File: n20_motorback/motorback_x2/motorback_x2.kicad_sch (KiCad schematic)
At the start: 13 parts, among them J1 Servo wire input, J2 Conn_01x01_Male, J3 Conn_01x01_Male, J4 prog_pins, U1 DRV8837DSGR, U2 ATtiny4-TS, U3 AIC1734-33GUTR

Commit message: mechanical improvements
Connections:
- net MOTORF: now also J4.5 (Pin_5), U2.1 (PB0); no longer J4.4 (Pin_4), U2.3 (PB1)
- net MOTORR: now also J4.4 (Pin_4), U2.3 (PB1); no longer J4.5 (Pin_5), U2.1 (PB0)
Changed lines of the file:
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@@
-    (stroke (width 0) (type solid) (color 0 0 0 0))
-  )
-  (wire (pts (xy 171.45 82.55) (xy 185.42 82.55))
     (stroke (width 0) (type solid) (color 0 0 0 0))
   )
@@
     (stroke (width 0) (type solid) (color 0 0 0 0))
   )
-  (wire (pts (xy 184.15 81.28) (xy 184.15 85.09))
+  (wire (pts (xy 180.975 81.28) (xy 180.975 82.55))
     (stroke (width 0) (type solid) (color 0 0 0 0))
   )
-  (wire (pts (xy 184.15 81.28) (xy 207.01 81.28))
+  (wire (pts (xy 180.975 81.28) (xy 207.01 81.28))
+    (stroke (width 0) (type solid) (color 0 0 0 0))
+  )
+  (wire (pts (xy 180.975 82.55) (xy 171.45 82.55))
+    (stroke (width 0) (type solid) (color 0 0 0 0))
+  )
+  (wire (pts (xy 184.15 83.82) (xy 184.15 85.09))
+    (stroke (width 0) (type solid) (color 0 0 0 0))
+  )
+  (wire (pts (xy 184.15 83.82) (xy 207.01 83.82))
     (stroke (width 0) (type solid) (color 0 0 0 0))
   )
   (wire (pts (xy 184.15 85.09) (xy 171.45 85.09))
-    (stroke (width 0) (type solid) (color 0 0 0 0))
-  )
-  (wire (pts (xy 185.42 82.55) (xy 185.42 83.82))
-    (stroke (width 0) (type solid) (color 0 0 0 0))
-  )
-  (wire (pts (xy 185.42 83.82) (xy 207.01 83.82))
     (stroke (width 0) (type solid) (color 0 0 0 0))
   )
@@
     (stroke (width 0) (type solid) (color 0 0 0 0))
   )
-  (text "PB0/ " (at 52.705 81.28 180)
+  (text "PB1/ " (at 53.34 81.28 180)
     (effects (font (size 1.27 1.27)) (justify right bottom))
   )
-  (text "PB1/ " (at 53.975 83.82 180)
+  (text "PB0/ " (at 53.34 83.82 180)
     (effects (font (size 1.27 1.27)) (justify right bottom))
   )
@@
     (effects (font (size 1.27 1.27)) (justify right bottom))
   )
-  (label "MOTORR" (at 45.72 81.28 180)
+  (label "MOTORF" (at 45.72 81.28 180)
     (effects (font (size 1.27 1.27)) (justify right bottom))
   )
-  (label "MOTORF" (at 46.355 83.82 180)
+  (label "MOTORR" (at 46.355 83.82 180)
     (effects (font (size 1.27 1.27)) (justify right bottom))
   )

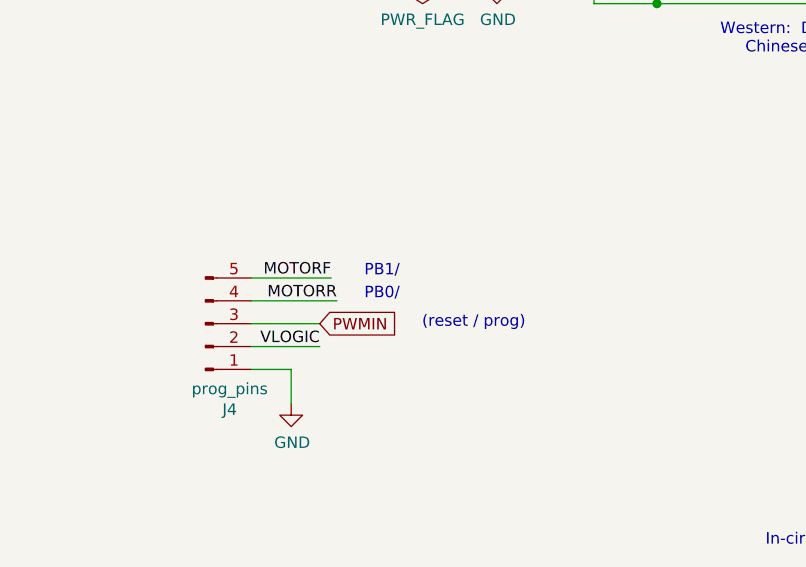
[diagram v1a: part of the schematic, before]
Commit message: Correct tpiclk / tpidata confusion
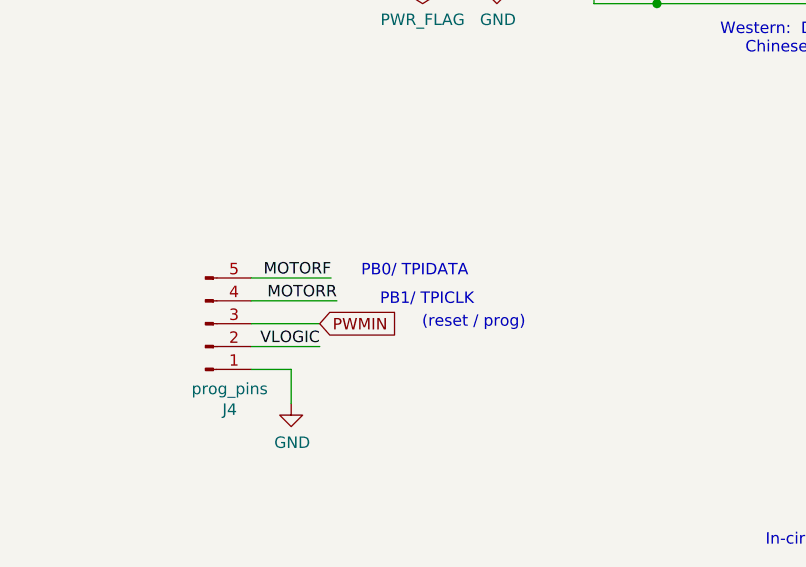
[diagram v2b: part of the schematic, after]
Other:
- note added: "PB0/ TPIDATA"
- note added: "PB1/ TPICLK"
- note removed: "PB0/"
- note removed: "PB1/"
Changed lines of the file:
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@@
     (stroke (width 0) (type solid) (color 0 0 0 0))
-  )
-  (text "PB1/ " (at 53.34 81.28 180)
-    (effects (font (size 1.27 1.27)) (justify right bottom))
-  )
-  (text "PB0/ " (at 53.34 83.82 180)
-    (effects (font (size 1.27 1.27)) (justify right bottom))
   )
   (text "Input servo connector" (at 55.88 33.02 180)
     (effects (font (size 1.27 1.27)) (justify right bottom))
   )
+  (text "PB0/ TPIDATA" (at 60.96 81.28 180)
+    (effects (font (size 1.27 1.27)) (justify right bottom))
+  )
+  (text "PB1/ TPICLK " (at 61.595 84.455 180)
+    (effects (font (size 1.27 1.27)) (justify right bottom))
+  )

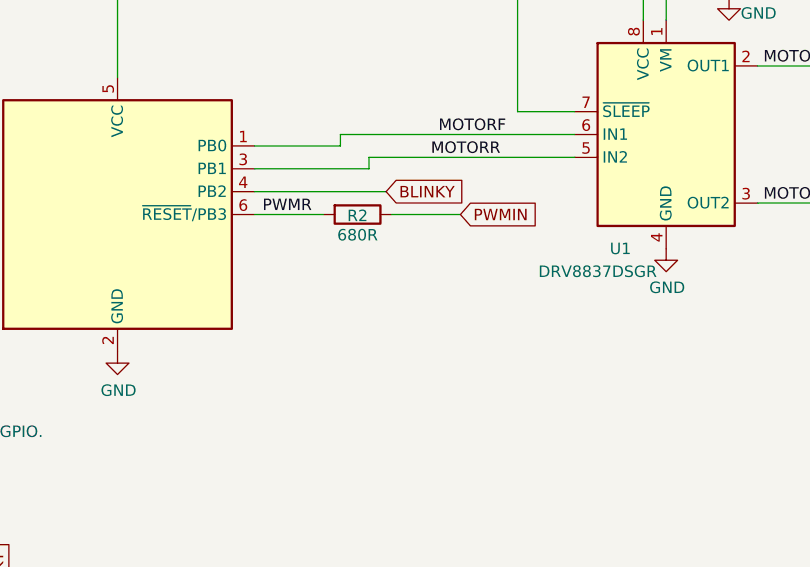
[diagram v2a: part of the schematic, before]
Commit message: Optional pull-down resistor
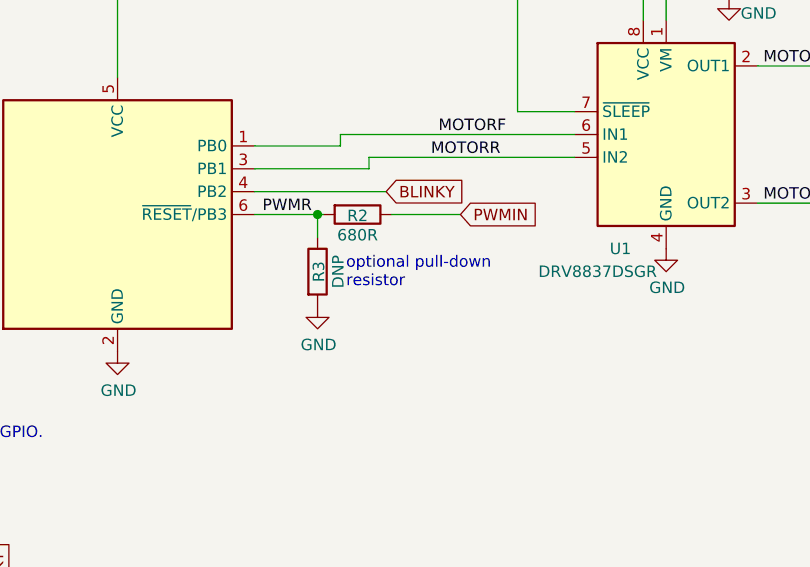
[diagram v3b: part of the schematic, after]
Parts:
- added R3: DNP, Resistor_SMD:R_0603_1608Metric, symbol Device:R
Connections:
- net GND: now also R3.2
- net PWMR: now also R3.1
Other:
- note added: "optional pull-down resistor"
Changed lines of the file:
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@@
   (junction (at 101.6 50.8) (diameter 1.016) (color 0 0 0 0))
   (junction (at 114.3 43.18) (diameter 1.016) (color 0 0 0 0))
+  (junction (at 178.435 90.17) (diameter 1.016) (color 0 0 0 0))
   (junction (at 200.66 63.5) (diameter 1.016) (color 0 0 0 0))
   (junction (at 224.155 58.42) (diameter 1.016) (color 0 0 0 0))
@@
     (stroke (width 0) (type solid) (color 0 0 0 0))
   )
-  (wire (pts (xy 171.45 90.17) (xy 179.07 90.17))
+  (wire (pts (xy 171.45 90.17) (xy 178.435 90.17))
+    (stroke (width 0) (type solid) (color 0 0 0 0))
+  )
+  (wire (pts (xy 178.435 90.17) (xy 178.435 92.71))
+    (stroke (width 0) (type solid) (color 0 0 0 0))
+  )
+  (wire (pts (xy 178.435 90.17) (xy 179.07 90.17))
     (stroke (width 0) (type solid) (color 0 0 0 0))
   )
@@
     (effects (font (size 1.27 1.27)) (justify right bottom))
   )
+  (text "optional pull-down\nresistor" (at 181.61 98.425 0)
+    (effects (font (size 1.27 1.27)) (justify left bottom))
+  )
   (label "VLOGIC" (at 44.45 88.9 180)
     (effects (font (size 1.27 1.27)) (justify right bottom))
@@
     )
     (property "Datasheet" "" (id 3) (at 156.21 105.41 0)
+      (effects (font (size 1.27 1.27)) hide)
+    )
+  )
+  (symbol (lib_id "power:GND") (at 178.435 100.33 0) (unit 1)
+    (in_bom yes) (on_board yes)
+    (property "Reference" "#PWR05" (id 0) (at 178.435 106.68 0)
+      (effects (font (size 1.27 1.27)) hide)
+    )
+    (property "Value" "GND" (id 1) (at 178.5493 104.6544 0))
+    (property "Footprint" "" (id 2) (at 178.435 100.33 0)
+      (effects (font (size 1.27 1.27)) hide)
+    )
+    (property "Datasheet" "" (id 3) (at 178.435 100.33 0)
       (effects (font (size 1.27 1.27)) hide)
     )
@@
     )
   )
+  (symbol (lib_id "Device:R") (at 178.435 96.52 0) (unit 1)
+    (in_bom yes) (on_board yes)
+    (property "Reference" "R3" (id 0) (at 178.5812 96.52 90))
+    (property "Value" "DNP" (id 1) (at 180.728 96.52 90))
+    (property "Footprint" "Resistor_SMD:R_0603_1608Metric" (id 2) (at 176.657 96.52 90)
+      (effects (font (size 1.27 1.27)) hide)
+    )
+    (property "Datasheet" "~" (id 3) (at 178.435 96.52 0)
+      (effects (font (size 1.27 1.27)) hide)
+    )
+    (property "LCSC" "" (id 4) (at 178.435 96.52 0)
+      (effects (font (size 1.27 1.27)) hide)
+    )
+  )
   (symbol (lib_id "Device:R") (at 182.88 90.17 270) (unit 1)
     (in_bom yes) (on_board yes)
@@
       (reference "#PWR04") (unit 1) (value "GND") (footprint "")
     )
+    (path "/3e975427-3807-4942-ac98-53614081a972"
+      (reference "#PWR05") (unit 1) (value "GND") (footprint "")
+    )
     (path "/6f1c6332-990d-4fb6-95f2-3c8294e6a89c"
       (reference "#PWR0101") (unit 1) (value "GND") (footprint "")
@@
       (reference "R2") (unit 1) (value "680R") (footprint "Resistor_SMD:R_0603_1608Metric")
     )
+    (path "/93d99eee-a5c7-43b8-b1f4-12240ff5256b"
+      (reference "R3") (unit 1) (value "DNP") (footprint "Resistor_SMD:R_0603_1608Metric")
+    )
     (path "/17f044cf-d669-4296-9d52-0d1ba68a5a56"

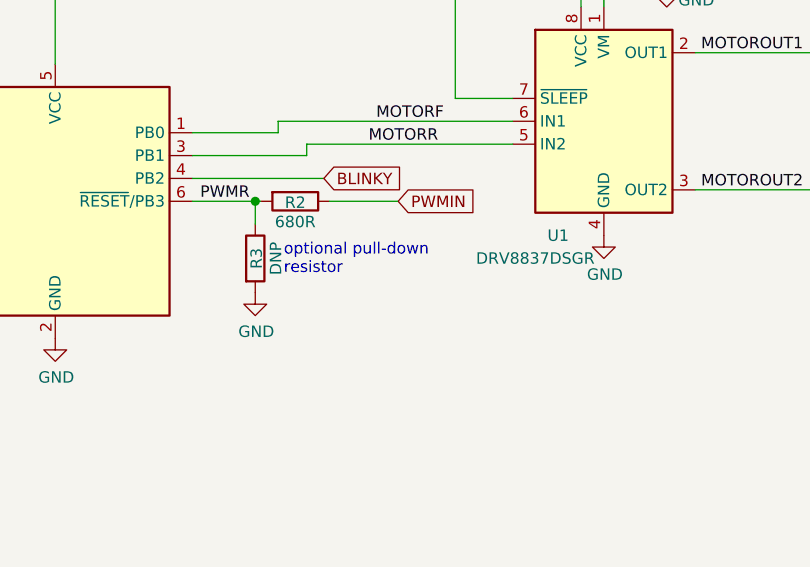
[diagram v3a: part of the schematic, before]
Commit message: remove unnecessary bits
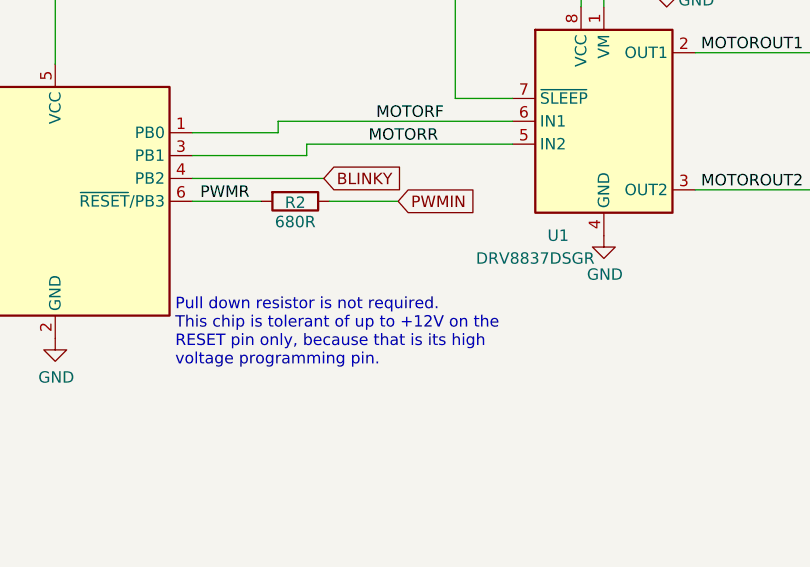
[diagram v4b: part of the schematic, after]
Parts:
- removed R3: DNP, Resistor_SMD:R_0603_1608Metric, symbol Device:R
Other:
- note added: "Pull down resistor is not required. This chip is tolerant of up to +12V on the RESET pin only, because that is its high voltage programming pin."
- note removed: "optional pull-down resistor"
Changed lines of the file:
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@@
   (junction (at 101.6 50.8) (diameter 1.016) (color 0 0 0 0))
   (junction (at 114.3 43.18) (diameter 1.016) (color 0 0 0 0))
-  (junction (at 178.435 90.17) (diameter 1.016) (color 0 0 0 0))
   (junction (at 200.66 63.5) (diameter 1.016) (color 0 0 0 0))
   (junction (at 224.155 58.42) (diameter 1.016) (color 0 0 0 0))
@@
     (stroke (width 0) (type solid) (color 0 0 0 0))
   )
-  (wire (pts (xy 171.45 90.17) (xy 178.435 90.17))
-    (stroke (width 0) (type solid) (color 0 0 0 0))
-  )
-  (wire (pts (xy 178.435 90.17) (xy 178.435 92.71))
-    (stroke (width 0) (type solid) (color 0 0 0 0))
-  )
-  (wire (pts (xy 178.435 90.17) (xy 179.07 90.17))
+  (wire (pts (xy 171.45 90.17) (xy 179.07 90.17))
     (stroke (width 0) (type solid) (color 0 0 0 0))
   )
@@
     (effects (font (size 1.27 1.27)) (justify right bottom))
   )
-  (text "optional pull-down\nresistor" (at 181.61 98.425 0)
+  (text "Pull down resistor is not required.\nThis chip is tolerant of up to +12V on the\nRESET pin only, because that is its high\nvoltage programming pin."
+    (at 169.545 108.585 0)
     (effects (font (size 1.27 1.27)) (justify left bottom))
   )
@@
     )
     (property "Datasheet" "" (id 3) (at 156.21 105.41 0)
-      (effects (font (size 1.27 1.27)) hide)
-    )
-  )
-  (symbol (lib_id "power:GND") (at 178.435 100.33 0) (unit 1)
-    (in_bom yes) (on_board yes)
-    (property "Reference" "#PWR05" (id 0) (at 178.435 106.68 0)
-      (effects (font (size 1.27 1.27)) hide)
-    )
-    (property "Value" "GND" (id 1) (at 178.5493 104.6544 0))
-    (property "Footprint" "" (id 2) (at 178.435 100.33 0)
-      (effects (font (size 1.27 1.27)) hide)
-    )
-    (property "Datasheet" "" (id 3) (at 178.435 100.33 0)
       (effects (font (size 1.27 1.27)) hide)
     )
@@
     )
   )
-  (symbol (lib_id "Device:R") (at 178.435 96.52 0) (unit 1)
-    (in_bom yes) (on_board yes)
-    (property "Reference" "R3" (id 0) (at 178.5812 96.52 90))
-    (property "Value" "DNP" (id 1) (at 180.728 96.52 90))
-    (property "Footprint" "Resistor_SMD:R_0603_1608Metric" (id 2) (at 176.657 96.52 90)
-      (effects (font (size 1.27 1.27)) hide)
-    )
-    (property "Datasheet" "~" (id 3) (at 178.435 96.52 0)
-      (effects (font (size 1.27 1.27)) hide)
-    )
-    (property "LCSC" "" (id 4) (at 178.435 96.52 0)
-      (effects (font (size 1.27 1.27)) hide)
-    )
-  )
   (symbol (lib_id "Device:R") (at 182.88 90.17 270) (unit 1)
     (in_bom yes) (on_board yes)
@@
       (reference "#PWR04") (unit 1) (value "GND") (footprint "")
     )
-    (path "/3e975427-3807-4942-ac98-53614081a972"
-      (reference "#PWR05") (unit 1) (value "GND") (footprint "")
-    )
     (path "/6f1c6332-990d-4fb6-95f2-3c8294e6a89c"
       (reference "#PWR0101") (unit 1) (value "GND") (footprint "")
@@
       (reference "R2") (unit 1) (value "680R") (footprint "Resistor_SMD:R_0603_1608Metric")
     )
-    (path "/93d99eee-a5c7-43b8-b1f4-12240ff5256b"
-      (reference "R3") (unit 1) (value "DNP") (footprint "Resistor_SMD:R_0603_1608Metric")
-    )
     (path "/17f044cf-d669-4296-9d52-0d1ba68a5a56"
